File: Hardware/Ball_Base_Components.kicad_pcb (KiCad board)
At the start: 4 copper layers, 92.3 x 128.5 mm, 77 parts, among them J1 Eurorack_10_pin_power, J2 SWD_Header, J3 USB_B_Micro, J4 X_Out, J5 Y_Out, J6 Z_Out, U1 STM32WB35, U2 LD1117-3.3-4Tab, U3 TL074, U4 TL072, Y1 32MHz

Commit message: PCB Updates
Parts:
- added G***: LOGO, Graphics:Ball, F.Cu at (80.3, 51.5)
- moved D5 1.40 mm to (129.7, 75.8)
- moved D6 1.40 mm to (129.7, 93.8)
- moved D4 1.40 mm to (129.7, 57.7)
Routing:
- net Net-(D6-Pad2): track 32.3 -> 30.9 mm
- net Net-(D6-Pad1): track 41.0 -> 39.6 mm
- net Net-(D5-Pad2): track 68.6 -> 67.2 mm
- net Net-(D4-Pad2): track 66.1 -> 65.0 mm
- net Net-(D4-Pad1): track 72.8 -> 72.2 mm
- net Net-(D5-Pad1): track 66.2 -> 65.6 mm
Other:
- outline, holes or cut-outs redrawn
- board text added: "Ball Panel v1.0"
- board text added: "Connect"
- board text added: "Mountjoy Modular"

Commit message: Remote schematic and PCB clean up
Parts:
- removed G***: LOGO, Graphics:Ball
- removed G***: LOGO, Custom_Footprints:bluetooth
- removed Ref** (x3): Thonkikonn_6.1mm, Custom_Footprints:MountingHole_6.1mm
- removed Ref** (x3): LED_Hole_3mm, Custom_Footprints:LED_Hole_3mm
- removed Ref** (x2): Oval_Mounting_Hole, Custom_Footprints:Oval_Mounting_Hole
- removed Ref** (x2): Push_Button_Hole, Custom_Footprints:Small_Pushbutton_Hole_3.5mm
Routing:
- removed copper zone on B.Cu, net (none)
- removed copper zone on F.Cu, net (none)
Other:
- board size 92.3 x 128.5 mm -> 40.6 x 100 mm
- board text removed: "Ball Panel v1.0"
- board text removed: "Connect"
- board text removed: "LED X"
- board text removed: "LED Y"
- board text removed: "LED Z"
- board text removed: "Mountjoy Modular"
- board text removed: "Reset"
- board text removed: "X Out"
- board text removed: "Y Out"
- board text removed: "Z Out"

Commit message: Preparation of Gerbers for manufacturing
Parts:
- moved C2 3.74 mm to (143.2, 140.6)
- moved C5 3.74 mm to (146.7, 143.8)
- moved C8 3.74 mm to (134.4, 150.5)
- moved D3 3.74 mm to (133.0, 140.0)
- moved L2 3.74 mm to (140.5, 137.6)
- moved R1 3.74 mm to (141.4, 140.6)
- moved U1 3.74 mm to (140.3, 146.6)
- moved Y1 3.74 mm to (137.9, 152.6)
- moved AE1 3.74 mm to (132.2, 147.8)
- moved C1 3.74 mm to (145.0, 140.6)
- moved C12 3.74 mm to (135.5, 147.4)
- moved C13 3.74 mm to (132.5, 147.3)
- moved C3 3.74 mm to (135.0, 145.6)
- moved C4 3.74 mm to (142.5, 152.5)
- moved C6 3.74 mm to (146.6, 147.8)
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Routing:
- net /USB_DP: track 17.7 -> 14.0 mm
- net /USB_DM: track 17.8 -> 14.1 mm
- net /SWIO: track 25.7 -> 22.1 mm
- net /X_PWM: track 14.7 -> 11.0 mm
- net /SWCLK: track 25.7 -> 22.0 mm
- net /Y_PWM: track 16.4 -> 13.2 mm
- net /CONNECT: track 14.7 -> 16.3 mm
- net /RESET: track 29.8 -> 31.2 mm
- net /Z_PWM: track 24.9 -> 25.5 mm
- net GND: vias 80 -> 84
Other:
- board size 40.6 x 100 mm -> 37 x 100 mm

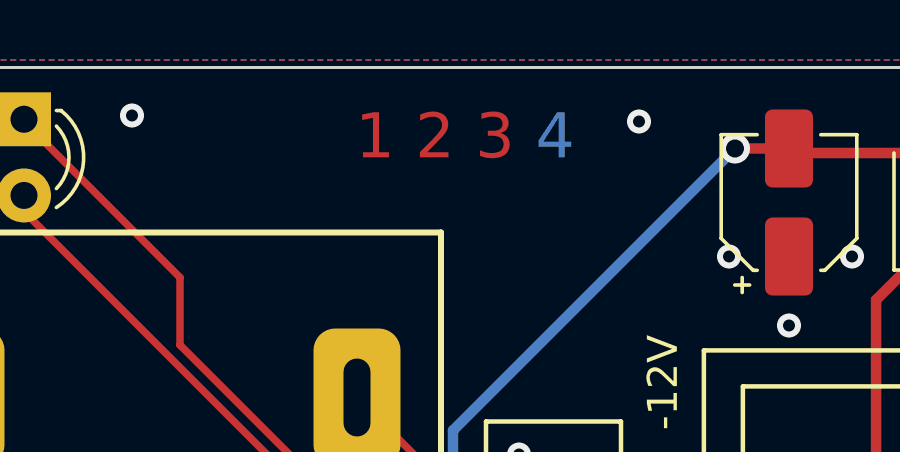
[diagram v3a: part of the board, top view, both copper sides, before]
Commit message: Fixed 4-layer marker incorrect copper layers
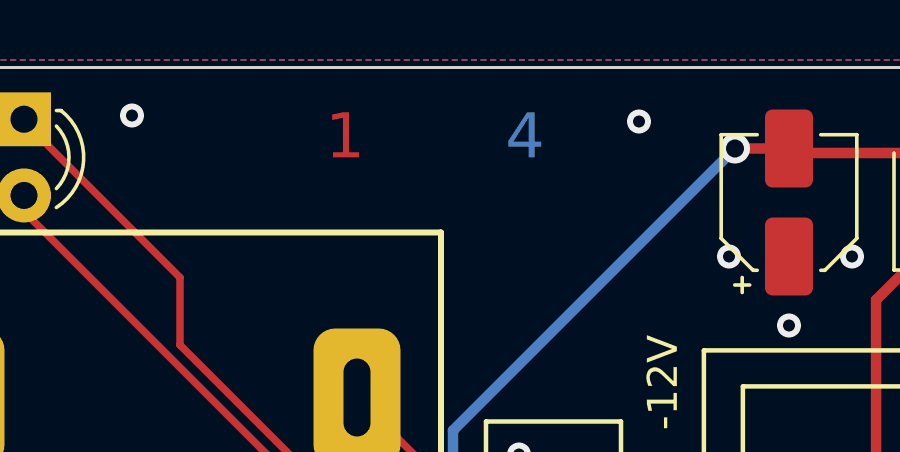
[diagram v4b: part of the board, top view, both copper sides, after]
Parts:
- moved FID1 1.00 mm to (143.4, 58.3)
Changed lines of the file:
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@@
+    )
+  )
+  (footprint "Custom_Footprints:4_Layer_Markers" (layer "F.Cu")
+    (at 143.4 58.3)
+    (property "Sheetfile" "Ball_Base_Components.kicad_sch")
+    (property "Sheetname" "")
+    (attr through_hole)
+    (fp_text reference "FID1" (at 0 4) (layer "F.SilkS") hide
+      (effects (font (size 1 1) (thickness 0.15)))
+    )
+    (fp_text value "4 Layer Marker" (at 0 -4) (layer "F.Fab")
+      (effects (font (size 1 1) (thickness 0.15)))
+    )
+    (fp_text user "1" (at -3 0) (layer "F.Cu")
+      (effects (font (size 1.5 1.5) (thickness 0.3)))
+    )
+    (fp_text user "2" (at -1 0) (layer "In1.Cu")
+      (effects (font (size 1.5 1.5) (thickness 0.3)))
+    )
+    (fp_text user "3" (at 1 0) (layer "In2.Cu")
+      (effects (font (size 1.5 1.5) (thickness 0.3)))
+    )
+    (fp_text user "4" (at 3 0) (layer "B.Cu")
+      (effects (font (size 1.5 1.5) (thickness 0.3)))
+    )
+    (fp_poly (pts
+        (xy 4 1)
+        (xy -4 1)
+        (xy -4 -1)
+        (xy 4 -1)
+      ) (layer "B.Mask") (width 0.1) (fill solid))
+    (fp_poly (pts
+        (xy 4 1)
+        (xy -4 1)
+        (xy -4 -1)
+        (xy 4 -1)
+      ) (layer "F.Mask") (width 0.1) (fill solid))
+    (zone (net 0) (net_name "") (layers *.Cu) (hatch edge 0.508)
+      (connect_pads (clearance 0))
+      (min_thickness 0.254)
+      (keepout (tracks not_allowed) (vias not_allowed) (pads not_allowed ) (copperpour not_allowed) (footprints allowed))
+      (fill (thermal_gap 0.508) (thermal_bridge_width 0.508))
+      (polygon
+        (pts
+          (xy 147.5 59.4)
+          (xy 139.3 59.4)
+          (xy 139.3 57.2)
+          (xy 147.5 57.2)
+        )
+      )
     )
   )
@@
     )
   )
-  (footprint "Custom_Footprints:4_Layer_Markers" (layer "F.Cu")
-    (at 144.4 58.3)
-    (property "Sheetfile" "Ball_Base_Components.kicad_sch")
-    (property "Sheetname" "")
-    (attr through_hole)
-    (fp_text reference "FID1" (at 0 4) (layer "F.SilkS") hide
-      (effects (font (size 1 1) (thickness 0.15)))
-    )
-    (fp_text value "4 Layer Marker" (at 0 -4) (layer "F.Fab")
-      (effects (font (size 1 1) (thickness 0.15)))
-    )
-    (fp_text user "1" (at -3 0) (layer "F.Cu")
-      (effects (font (size 1.5 1.5) (thickness 0.3)))
-    )
-    (fp_text user "3" (at 1 0) (layer "F.Cu")
-      (effects (font (size 1.5 1.5) (thickness 0.3)))
-    )
-    (fp_text user "2" (at -1 0) (layer "F.Cu")
-      (effects (font (size 1.5 1.5) (thickness 0.3)))
-    )
-    (fp_text user "4" (at 3 0) (layer "B.Cu")
-      (effects (font (size 1.5 1.5) (thickness 0.3)))
-    )
-    (fp_poly (pts
-        (xy 4 1)
-        (xy -4 1)
-        (xy -4 -1)
-        (xy 4 -1)
-      ) (layer "B.Mask") (width 0.1) (fill solid))
-    (fp_poly (pts
-        (xy 4 1)
-        (xy -4 1)
-        (xy -4 -1)
-        (xy 4 -1)
-      ) (layer "F.Mask") (width 0.1) (fill solid))
-    (zone (net 0) (net_name "") (layers *.Cu) (hatch edge 0.508)
-      (connect_pads (clearance 0))
-      (min_thickness 0.254)
-      (keepout (tracks not_allowed) (vias not_allowed) (pads not_allowed ) (copperpour not_allowed) (footprints allowed))
-      (fill (thermal_gap 0.508) (thermal_bridge_width 0.508))
-      (polygon
-        (pts
-          (xy 148.5 59.4)
-          (xy 140.3 59.4)
-          (xy 140.3 57.2)
-          (xy 148.5 57.2)
-        )
-      )
-    )
-  )
